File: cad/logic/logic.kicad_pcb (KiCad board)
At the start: 2 copper layers, 70 x 52 mm, 15 parts, among them J1 Conn_01x06, J2 Conn_01x02, J3 Conn_01x02, J4 Conn_01x02, J5 Conn_01x02, J6 Conn_01x02, J7 Conn_01x02, J8 Conn_01x02, J9 Conn_01x02, U1 74HC595, U2 TPL7407LAD, U3 TPL7407LAD, U4 TPL7407LAD

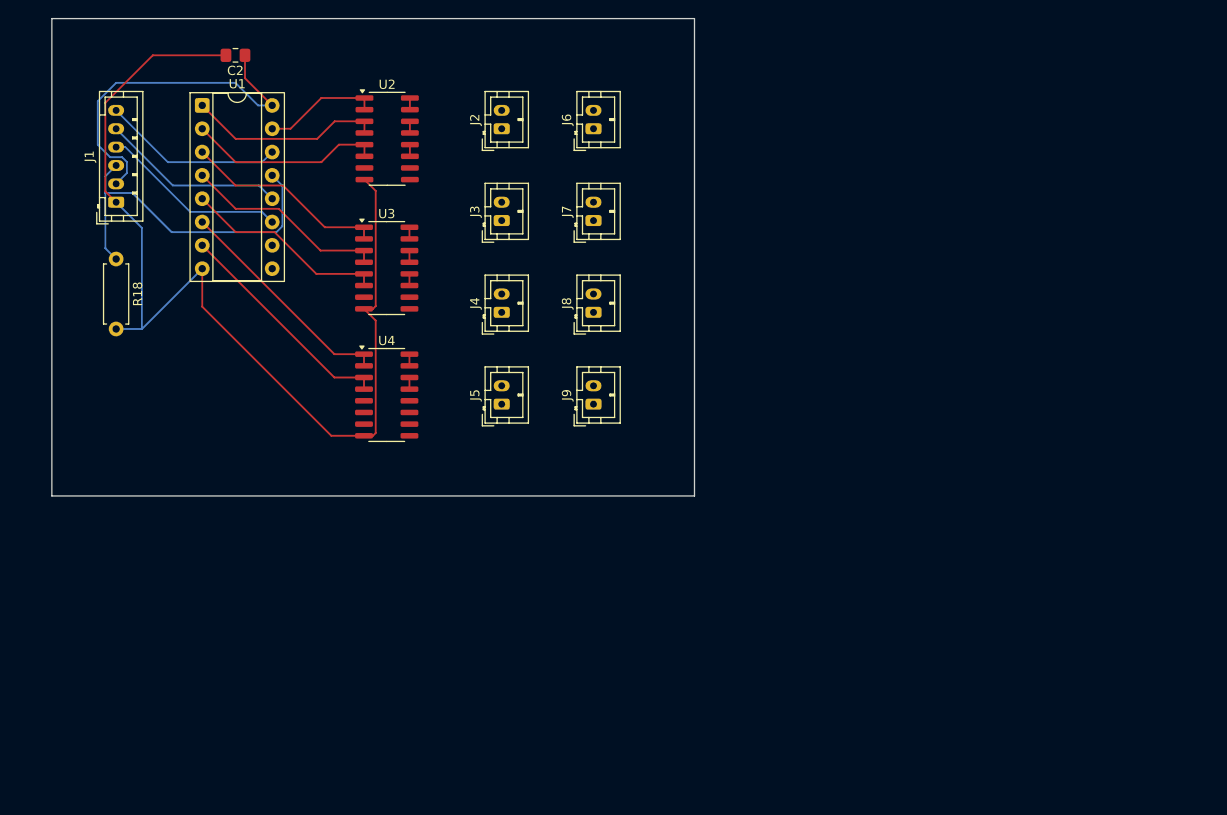
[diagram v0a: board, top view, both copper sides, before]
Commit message: Simplified schema and wired PCB
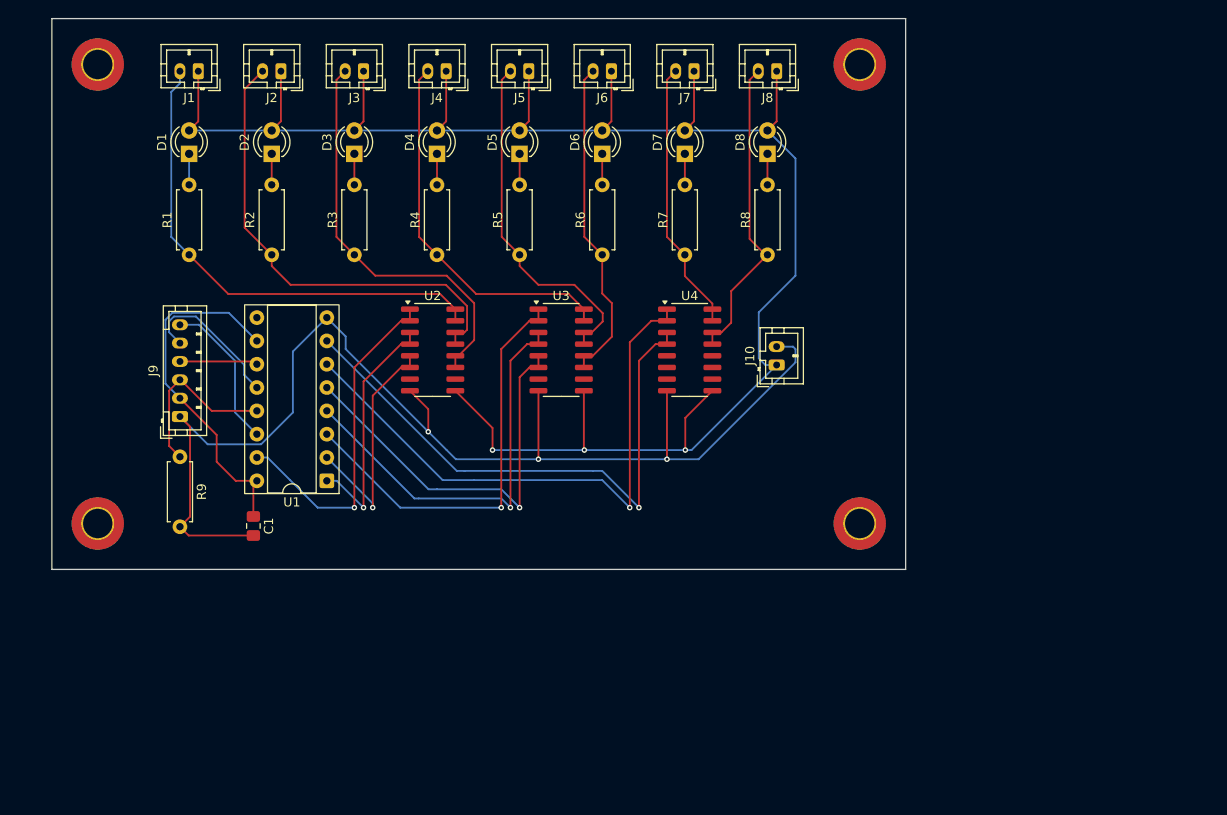
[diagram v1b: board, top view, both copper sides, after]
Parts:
- added D1: LED, LED_THT:LED_D3.0mm, F.Cu at (40.0, 36.7)
- added D2: LED, LED_THT:LED_D3.0mm, F.Cu at (49.0, 36.7)
- added D3: LED, LED_THT:LED_D3.0mm, F.Cu at (58.0, 36.7)
- added D4: LED, LED_THT:LED_D3.0mm, F.Cu at (67.0, 36.7)
- added D5: LED, LED_THT:LED_D3.0mm, F.Cu at (76.0, 36.7)
- added D6: LED, LED_THT:LED_D3.0mm, F.Cu at (85.0, 36.7)
- added D7: LED, LED_THT:LED_D3.0mm, F.Cu at (94.0, 36.7)
- added D8: LED, LED_THT:LED_D3.0mm, F.Cu at (103.0, 36.7)
- added J10: Conn_01x02, Connector_JST:JST_PH_B2B-PH-K_1x02_P2.00mm_Vertical, F.Cu at (104.0, 59.7)
- added M3: MountingHole_3.2mm_M3_ISO7380_Pad_TopBottom, MountingHole:MountingHole_3.2mm_M3_ISO7380_Pad_TopBottom, F.Cu at (113.0, 27.0)
- added M3: MountingHole_3.2mm_M3_ISO7380_Pad_TopBottom, MountingHole:MountingHole_3.2mm_M3_ISO7380_Pad_TopBottom, F.Cu at (113.0, 77.0)
- added M3: MountingHole_3.2mm_M3_ISO7380_Pad_TopBottom, MountingHole:MountingHole_3.2mm_M3_ISO7380_Pad_TopBottom, F.Cu at (30.0, 77.0)
- added M3: MountingHole_3.2mm_M3_ISO7380_Pad_TopBottom, MountingHole:MountingHole_3.2mm_M3_ISO7380_Pad_TopBottom, F.Cu at (30.0, 27.0)
- added R1: 1k, Resistor_THT:R_Axial_DIN0207_L6.3mm_D2.5mm_P7.62mm_Horizontal, F.Cu at (40.0, 47.7)
- added R2: 1k, Resistor_THT:R_Axial_DIN0207_L6.3mm_D2.5mm_P7.62mm_Horizontal, F.Cu at (49.0, 47.7)
- added R3: 1k, Resistor_THT:R_Axial_DIN0207_L6.3mm_D2.5mm_P7.62mm_Horizontal, F.Cu at (58.0, 47.7)
- added R4: 1k, Resistor_THT:R_Axial_DIN0207_L6.3mm_D2.5mm_P7.62mm_Horizontal, F.Cu at (67.0, 47.7)
- added R5: 1k, Resistor_THT:R_Axial_DIN0207_L6.3mm_D2.5mm_P7.62mm_Horizontal, F.Cu at (76.0, 47.7)
- added R6: 1k, Resistor_THT:R_Axial_DIN0207_L6.3mm_D2.5mm_P7.62mm_Horizontal, F.Cu at (85.0, 47.7)
- added R7: 1k, Resistor_THT:R_Axial_DIN0207_L6.3mm_D2.5mm_P7.62mm_Horizontal, F.Cu at (94.0, 47.7)
- added R8: 1k, Resistor_THT:R_Axial_DIN0207_L6.3mm_D2.5mm_P7.62mm_Horizontal, F.Cu at (103.0, 47.7)
- moved C1 51.3 mm to (47.0, 77.3), turned to -90 degrees
- moved U1 43.1 mm to (55.0, 72.3), turned to 180 degrees
- moved J8 41.4 mm to (104.0, 27.7), turned to 180 degrees
- moved J4 36.8 mm to (68.0, 27.7), turned to 180 degrees
- moved J1 33.6 mm to (41.0, 27.7), turned to 180 degrees
- moved U4 33.4 mm to (94.5, 58.1)
- moved J3 30.3 mm to (59.0, 27.7), turned to 180 degrees
- moved J2 29.0 mm to (50.0, 27.7), turned to 180 degrees
- moved J7 28.5 mm to (95.0, 27.7), turned to 180 degrees
- moved J9 24.4 mm to (39.0, 65.3)
- moved U2 23.5 mm to (66.5, 58.1)
- moved R9 22.6 mm to (39.0, 69.7)
- moved U3 21.0 mm to (80.5, 58.1)
- moved J6 16.4 mm to (86.0, 27.7), turned to 180 degrees
- moved J5 9.43 mm to (77.0, 27.7), turned to 180 degrees
- renumbered C2 to C1, J2 to J1, J3 to J2, J4 to J3, J5 to J4, J6 to J5, J7 to J6, J8 to J7, J9 to J8, J1 to J9, R18 to R9
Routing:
- net +12V: track 0.00 -> 205.1 mm, vias 0 -> 3
- net Net-(J1-Pin_2): track 1.27 -> 53.9 mm
- net Net-(J2-Pin_2): track 1.27 -> 51.6 mm
- net Net-(J3-Pin_2): track 1.27 -> 44.5 mm
- net Net-(J4-Pin_2): track 1.27 -> 40.9 mm
- net Net-(U1-QG): track 24.9 -> 63.8 mm, vias 0 -> 1
- net Net-(U1-QH): track 24.9 -> 62.6 mm, vias 0 -> 1
- net Net-(J5-Pin_2): track 1.27 -> 38.3 mm
- net Net-(J6-Pin_2): track 1.27 -> 35.7 mm
- net Net-(J8-Pin_2): track 1.27 -> 34.1 mm
- net Net-(J7-Pin_2): track 1.27 -> 29.6 mm
- net Net-(U1-QA): track 12.7 -> 37.6 mm, vias 0 -> 1
- net Net-(U1-QD): track 22.3 -> 46.2 mm, vias 0 -> 1
- net Net-(U1-QE): track 22.3 -> 45.4 mm, vias 0 -> 1
- net GND: track 112.4 -> 134.6 mm, vias 0 -> 3
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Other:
- board size 70 x 52 mm -> 93 x 60 mm

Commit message: Initial design complete
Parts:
- added A1: Arduino_Nano_ESP32, Module:Arduino_Nano, F.Cu at (64.3, 57.2)
- added C2: 100nF, Capacitor_THT:C_Disc_D4.7mm_W2.5mm_P5.00mm, F.Cu at (124.4, 52.6)
- added C3: 100nF, Capacitor_THT:C_Disc_D4.7mm_W2.5mm_P5.00mm, F.Cu at (76.7, 70.1)
- added C4: 100nF, Capacitor_THT:C_Disc_D4.7mm_W2.5mm_P5.00mm, F.Cu at (64.3, 77.2)
- added J11: Conn_01x04, Connector_JST:JST_PH_B4B-PH-K_1x04_P2.00mm_Vertical, F.Cu at (57.7, 99.6)
- added J12: Conn_01x04, Connector_JST:JST_PH_B4B-PH-K_1x04_P2.00mm_Vertical, F.Cu at (69.7, 99.6)
- added J13: Conn_01x04, Connector_JST:JST_PH_B4B-PH-K_1x04_P2.00mm_Vertical, F.Cu at (81.7, 99.6)
- added J14: Conn_01x04, Connector_JST:JST_PH_B4B-PH-K_1x04_P2.00mm_Vertical, F.Cu at (93.7, 99.6)
- added J15: Conn_01x04, Connector_JST:JST_PH_B4B-PH-K_1x04_P2.00mm_Vertical, F.Cu at (105.7, 99.6)
- added J16: Conn_01x04, Connector_JST:JST_PH_B4B-PH-K_1x04_P2.00mm_Vertical, F.Cu at (117.7, 99.6)
- added J17: Conn_01x04, Connector_JST:JST_PH_B4B-PH-K_1x04_P2.00mm_Vertical, F.Cu at (129.7, 99.6)
- added R10: 100R, Resistor_THT:R_Axial_DIN0207_L6.3mm_D2.5mm_P7.62mm_Horizontal, F.Cu at (116.9, 46.5)
- added R11: 100R, Resistor_THT:R_Axial_DIN0207_L6.3mm_D2.5mm_P7.62mm_Horizontal, F.Cu at (128.9, 46.5)
- C1: footprint Capacitor_SMD:C_0805_2012Metric_Pad1.18x1.45mm_HandSolder -> Capacitor_THT:C_Disc_D4.7mm_W2.5mm_P5.00mm
- J10: value Conn_01x02 -> Conn_01x04; footprint Connector_JST:JST_PH_B2B-PH-K_1x02_P2.00mm_Vertical -> Connector_JST:JST_PH_B4B-PH-K_1x04_P2.00mm_Vertical
- J9: value Conn_01x06 -> Barrel_Jack_Switch; footprint Connector_JST:JST_PH_B6B-PH-K_1x06_P2.00mm_Vertical -> Connector_BarrelJack:BarrelJack_Horizontal
- R1, R2, R3: value 1k -> 10k
- R4, R5, R6, R7, R8: value 1k -> 100R
- R9: value 10k -> 100R
- U1: value 74HC595 -> R-78E5.0-1.0; footprint Package_DIP:DIP-16_W7.62mm_Socket -> Converter_DCDC:Converter_DCDC_RECOM_R-78E-0.5_THT
- U2: value TPL7407LAD -> 74HC595; footprint Package_SO:SOIC-16_3.9x9.9mm_P1.27mm -> Package_DIP:DIP-16_W7.62mm_Socket
- U3: value TPL7407LAD -> TBD62381APG; footprint Package_SO:SOIC-16_3.9x9.9mm_P1.27mm -> footprints:P-DIP18-300-2p54-001_TOS
- U4: value TPL7407LAD -> TCA9548APWR; footprint Package_SO:SOIC-16_3.9x9.9mm_P1.27mm -> Package_DIP:DIP-24_18.0mmx34.29mm_W15.24mm_Socket
- moved M4 117.4 mm to (144.9, 100.7)
- moved M3 85.4 mm to (31.0, 100.7)
- moved J10 70.5 mm to (45.7, 99.6), turned to 0 degrees
- moved R9 69.9 mm to (104.9, 46.5), turned to 0 degrees
- moved R2 47.6 mm to (96.3, 52.6), turned to 0 degrees
- moved R1 45.5 mm to (85.2, 52.6), turned to 0 degrees
- moved R3 43.5 mm to (69.6, 89.7)
- moved C1 38.7 mm to (76.7, 52.6), turned to 0 degrees
- moved U4 36.2 mm to (76.7, 89.7), turned to 90 degrees
- moved M2 32.3 mm to (144.9, 31.5)
- moved D8 31.4 mm to (134.0, 41.3), turned to 180 degrees
- moved D7 28.4 mm to (122.0, 41.3), turned to 180 degrees
- moved J8 27.9 mm to (131.7, 30.5), turned to 0 degrees
- moved D6 25.5 mm to (110.0, 41.3), turned to 180 degrees
- moved J7 24.9 mm to (119.7, 30.5), turned to 0 degrees
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- renumbered M3 to M1, M3 to M2, M3 to M4
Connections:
- D1 pad 2: +12V -> Net-(D1-A)
- D2 pad 2: +12V -> Net-(D2-A)
- D3 pad 2: +12V -> Net-(D3-A)
- D4 pad 2: +12V -> Net-(D4-A)
- D5 pad 2: +12V -> Net-(D5-A)
- D6 pad 2: +12V -> Net-(D6-A)
- D7 pad 2: +12V -> Net-(D7-A)
- D8 pad 2: +12V -> Net-(D8-A)
- J1 pad 2: Net-(J1-Pin_2) -> Net-(D1-K)
- J10 pad 1: +12V -> Net-(J10-Pin_1)
- J10 pad 2: GND -> Net-(J10-Pin_2)
- J2 pad 2: Net-(J2-Pin_2) -> Net-(D2-K)
- J3 pad 2: Net-(J3-Pin_2) -> Net-(D3-K)
- J4 pad 2: Net-(J4-Pin_2) -> Net-(D4-K)
- J5 pad 2: Net-(J5-Pin_2) -> Net-(D5-K)
- J6 pad 2: Net-(J6-Pin_2) -> Net-(D6-K)
- J7 pad 2: Net-(J7-Pin_2) -> Net-(D7-K)
- J8 pad 2: Net-(J8-Pin_2) -> Net-(D8-K)
- J9 pad 1: GND -> +12V
- J9 pad 2: +5V -> GND
- J9 pad 3: Net-(J9-Pin_3) -> unconnected-(J9-Pad3)
- R1 pad 1: Net-(J1-Pin_2) -> Net-(A1-D5)
- R1 pad 2: Net-(D1-K) -> GND
- R2 pad 1: Net-(J2-Pin_2) -> Net-(A1-D2)
- R2 pad 2: Net-(D2-K) -> +5V
- R3 pad 1: Net-(J3-Pin_2) -> Net-(A1-D7)
- R3 pad 2: Net-(D3-K) -> +5V
- R4 pad 1: Net-(J4-Pin_2) -> Net-(D1-A)
- R4 pad 2: Net-(D4-K) -> +12V
- R5 pad 1: Net-(J5-Pin_2) -> Net-(D2-A)
- R5 pad 2: Net-(D5-K) -> +12V
- R6 pad 1: Net-(J6-Pin_2) -> Net-(D3-A)
- R6 pad 2: Net-(D6-K) -> +12V
- R7 pad 1: Net-(J7-Pin_2) -> Net-(D4-A)
- R7 pad 2: Net-(D7-K) -> +12V
- R8 pad 1: Net-(J8-Pin_2) -> Net-(D5-A)
- R8 pad 2: Net-(D8-K) -> +12V
- R9 pad 1: Net-(J9-Pin_3) -> Net-(D6-A)
- R9 pad 2: GND -> +12V
- U1 pad 1: Net-(U1-QB) -> +12V
- U1 pad 2: Net-(U1-QC) -> GND
- U1 pad 3: Net-(U1-QD) -> +5V
- U2 pad 1: Net-(U1-QA) -> Net-(U2-QB)
- U2 pad 10: unconnected-(U2-OUT7-Pad10) -> Net-(A1-D2)
- U2 pad 11: Net-(J3-Pin_2) -> Net-(A1-D3)
- U2 pad 12: Net-(J3-Pin_2) -> Net-(A1-D4)
- U2 pad 13: Net-(J2-Pin_2) -> Net-(A1-D5)
- U2 pad 14: Net-(J2-Pin_2) -> Net-(A1-D6)
- U2 pad 15: Net-(J1-Pin_2) -> Net-(U2-QA)
- U2 pad 16: Net-(J1-Pin_2) -> +5V
- U2 pad 2: Net-(U1-QA) -> Net-(U2-QC)
- U2 pad 3: Net-(U1-QB) -> Net-(U2-QD)
- U2 pad 4: Net-(U1-QB) -> Net-(U2-QE)
- U2 pad 5: Net-(U1-QC) -> Net-(U2-QF)
- U2 pad 6: Net-(U1-QC) -> Net-(U2-QG)
- U2 pad 7: unconnected-(U2-IN7-Pad7) -> Net-(U2-QH)
- U2 pad 9: +12V -> unconnected-(U2-QH&apos;-Pad9)
- U3 pad 1: Net-(U1-QD) -> Net-(U2-QA)
- U3 pad 10: unconnected-(U3-OUT7-Pad10) -> +5V
- U3 pad 11: Net-(J6-Pin_2) -> Net-(D8-K)
- U3 pad 12: Net-(J6-Pin_2) -> Net-(D7-K)
- U3 pad 13: Net-(J5-Pin_2) -> Net-(D6-K)
- U3 pad 14: Net-(J5-Pin_2) -> Net-(D5-K)
- U3 pad 15: Net-(J4-Pin_2) -> Net-(D4-K)
- U3 pad 16: Net-(J4-Pin_2) -> Net-(D3-K)
- U3 pad 2: Net-(U1-QD) -> Net-(U2-QB)
- U3 pad 3: Net-(U1-QE) -> Net-(U2-QC)
- U3 pad 4: Net-(U1-QE) -> Net-(U2-QD)
- U3 pad 5: Net-(U1-QF) -> Net-(U2-QE)
- U3 pad 6: Net-(U1-QF) -> Net-(U2-QF)
- U3 pad 7: unconnected-(U3-IN7-Pad7) -> Net-(U2-QG)
- U3 pad 8: GND -> Net-(U2-QH)
- U3 pad 9: +12V -> GND
- U4 pad 1: Net-(U1-QG) -> unconnected-(U4-A0-Pad1)
- U4 pad 10: unconnected-(U4-OUT7-Pad10) -> Net-(J13-Pin_2)
- U4 pad 11: unconnected-(U4-OUT6-Pad11) -> Net-(J13-Pin_1)
- U4 pad 12: unconnected-(U4-OUT5-Pad12) -> GND
- U4 pad 13: Net-(J8-Pin_2) -> Net-(J14-Pin_2)
- U4 pad 14: Net-(J8-Pin_2) -> Net-(J14-Pin_1)
- U4 pad 15: Net-(J7-Pin_2) -> Net-(J15-Pin_2)
- U4 pad 16: Net-(J7-Pin_2) -> Net-(J15-Pin_1)
- U4 pad 2: Net-(U1-QG) -> unconnected-(U4-A1-Pad2)
- U4 pad 3: Net-(U1-QH) -> Net-(A1-D7)
- U4 pad 4: Net-(U1-QH) -> Net-(J10-Pin_2)
- U4 pad 5: unconnected-(U4-IN5-Pad5) -> Net-(J10-Pin_1)
- U4 pad 6: unconnected-(U4-IN6-Pad6) -> Net-(J11-Pin_2)
- U4 pad 7: unconnected-(U4-IN7-Pad7) -> Net-(J11-Pin_1)
- U4 pad 8: GND -> Net-(J12-Pin_2)
- U4 pad 9: +12V -> Net-(J12-Pin_1)
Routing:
- net +5V: track 38.6 -> 317.0 mm, vias 0 -> 1
- net GND: track 134.6 -> 316.3 mm, vias 3 -> 1
- net +12V: track 205.1 -> 384.4 mm, vias 3 -> 0
- net Net-(J14-Pin_2): track 0.00 -> 106.0 mm
- net Net-(J14-Pin_1): track 0.00 -> 101.4 mm
- net Net-(J15-Pin_2): track 0.00 -> 96.4 mm
- net Net-(J15-Pin_1): track 0.00 -> 91.8 mm
- net Net-(J16-Pin_2): track 0.00 -> 86.8 mm
- net Net-(J16-Pin_1): track 0.00 -> 82.2 mm
- net Net-(J17-Pin_2): track 0.00 -> 77.2 mm
- net Net-(J17-Pin_1): track 0.00 -> 72.7 mm
- net Net-(D1-K): track 3.38 -> 73.6 mm
- net Net-(A1-D7): track 0.00 -> 68.9 mm
- net Net-(U1-QG): track 63.8 -> 0.00 mm, vias 1 -> 0
- net Net-(U1-QH): track 62.6 -> 0.00 mm, vias 1 -> 0
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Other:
- board size 93 x 60 mm -> 125.9 x 81.3 mm

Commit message: Added capacitor
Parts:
- added C5: 20µF, Capacitor_THT:C_Disc_D4.7mm_W2.5mm_P5.00mm, F.Cu at (51.4, 77.2)
- U3: footprint footprints:P-DIP18-300-2p54-001_TOS -> Package_DIP:CERDIP-18_W7.62mm_SideBrazed_Socket
- moved U1 3.81 mm to (46.0, 85.1)
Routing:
- net +5V: track 317.0 -> 324.3 mm
- net GND: track 316.3 -> 319.6 mm
- net Net-(A1-D7): track 68.9 -> 70.9 mm
